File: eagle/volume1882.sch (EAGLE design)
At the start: 39 parts, among them IC1 LM317, IC2 LM337, U1 DS1882, U2 ATMEGA328P_TQFP

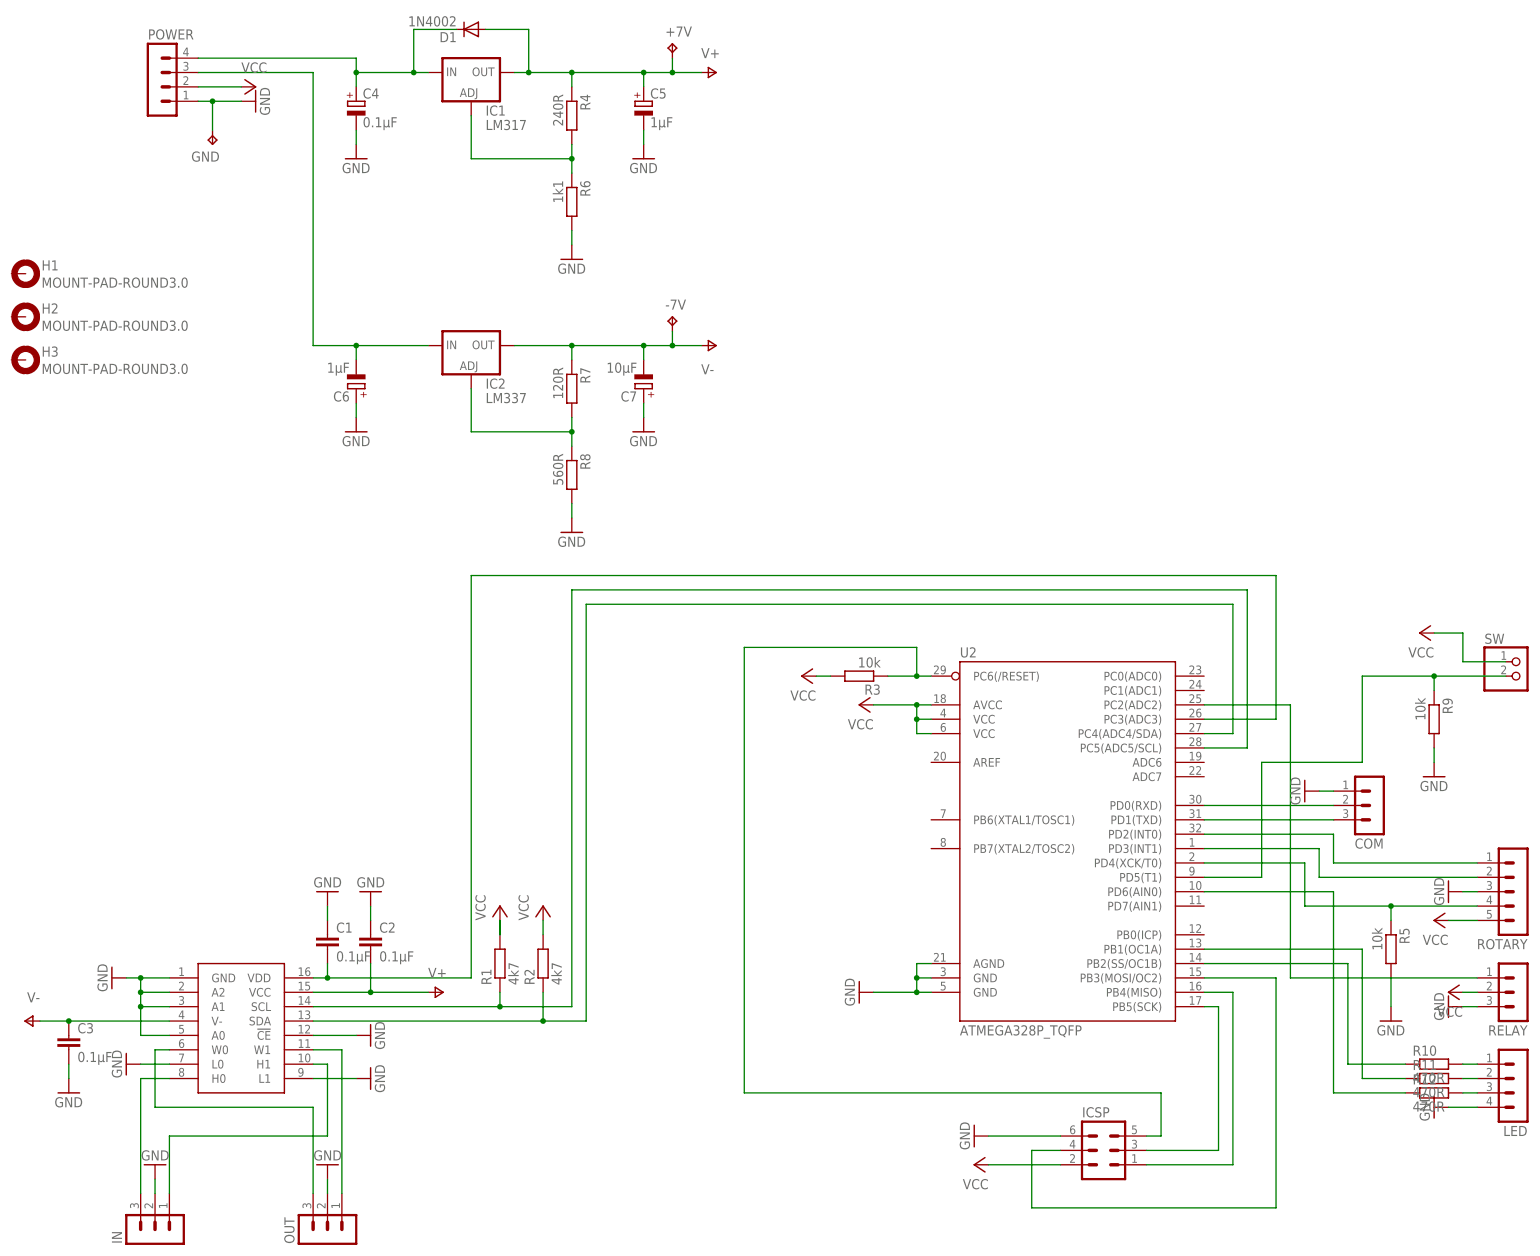
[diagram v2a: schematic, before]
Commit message: fixed wrong size parts
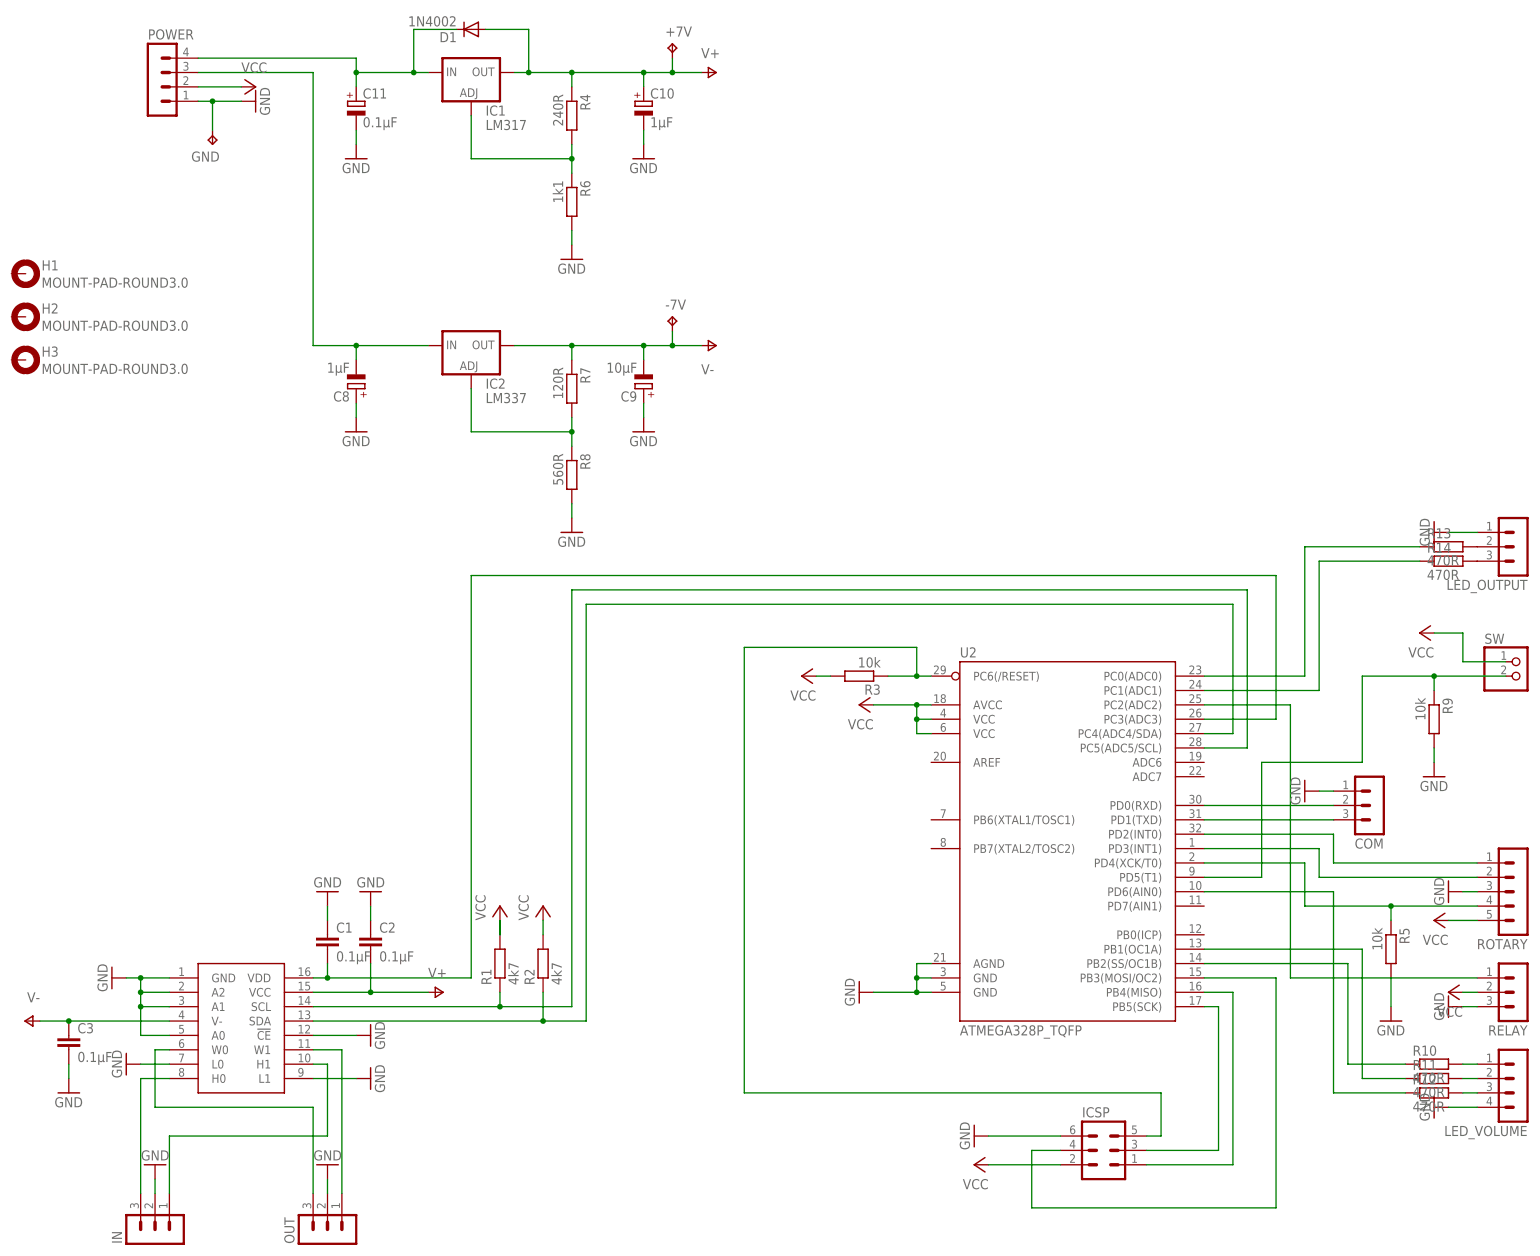
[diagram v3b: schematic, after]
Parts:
- removed C4: 0.1µF, resistor:CPOL-EUE5-5
- removed C5, C6: 1µF, resistor:CPOL-EUE5-5
- removed C7: 10µF, resistor:CPOL-EUE5-5
- added C10, C8: 1µF, resistor:CPOL-EUE2-5
- added C11: 0.1µF, resistor:CPOL-EUE2-5
- added C9: 10µF, resistor:CPOL-EUE2-5
- added LED_OUTPUT: (no value), con-lstb:MA03-1
- added R13, R14: 470R, resistor:R-EU_R1206
- renumbered LED to LED_VOLUME
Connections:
- new net N$29: R13.1, U2.PC0(ADC0)
- new net N$30: R14.1, U2.PC1(ADC1)
- new net N$31: LED_OUTPUT.2, R13.2
- new net N$32: LED_OUTPUT.3, R14.2
- net GND: now also C10.-, C11.-, C8.+, C9.+, LED_OUTPUT.1; no longer C4.-, C5.-, C6.+, C7.+
- net N$20: now also C11.+; no longer C4.+
- net N$21: now also C8.-; no longer C6.-
- net V+: now also C10.+; no longer C5.+
- net V-: now also C9.-; no longer C7.-
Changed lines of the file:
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@@
 <part name="R5" library="resistor" deviceset="R-EU_" device="R1206" value="10k"/>
 <part name="P+9" library="supply1" deviceset="VCC" device=""/>
-<part name="LED" library="con-lstb" deviceset="MA04-1" device=""/>
+<part name="LED_VOLUME" library="con-lstb" deviceset="MA04-1" device=""/>
 <part name="GND11" library="supply1" deviceset="GND" device=""/>
 <part name="IN" library="con-lstb" deviceset="MA03-1" device=""/>
@@
 <part name="IC1" library="v-reg" deviceset="LM317?*" device="MBSTT3" value="LM317"/>
 <part name="POWER" library="con-lstb" deviceset="MA04-1" device=""/>
-<part name="C4" library="resistor" deviceset="CPOL-EU" device="E5-5" value="0.1µF"/>
-<part name="C5" library="resistor" deviceset="CPOL-EU" device="E5-5" value="1µF"/>
 <part name="GND16" library="supply1" deviceset="GND" device=""/>
 <part name="GND17" library="supply1" deviceset="GND" device=""/>
@@
 <part name="P+8" library="supply1" deviceset="VCC" device=""/>
 <part name="IC2" library="lm337" deviceset="LM337" device=""/>
-<part name="C6" library="resistor" deviceset="CPOL-EU" device="E5-5" value="1µF"/>
-<part name="C7" library="resistor" deviceset="CPOL-EU" device="E5-5" value="10µF"/>
 <part name="GND20" library="supply1" deviceset="GND" device=""/>
 <part name="GND21" library="supply1" deviceset="GND" device=""/>
@@
 <part name="+7V" library="testpad" deviceset="TP" device="TP12SQ"/>
 <part name="GND" library="testpad" deviceset="TP" device="TP12SQ"/>
+<part name="LED_OUTPUT" library="con-lstb" deviceset="MA03-1" device=""/>
+<part name="GND25" library="supply1" deviceset="GND" device=""/>
+<part name="R13" library="resistor" deviceset="R-EU_" device="R1206" value="470R"/>
+<part name="R14" library="resistor" deviceset="R-EU_" device="R1206" value="470R"/>
+<part name="C8" library="resistor" deviceset="CPOL-EU" device="E2-5" value="1µF"/>
+<part name="C9" library="resistor" deviceset="CPOL-EU" device="E2-5" value="10µF"/>
+<part name="C10" library="resistor" deviceset="CPOL-EU" device="E2-5" value="1µF"/>
+<part name="C11" library="resistor" deviceset="CPOL-EU" device="E2-5" value="0.1µF"/>
 </parts>
 <sheets>
@@
 <instance part="R5" gate="G$1" x="231.14" y="50.8" rot="R270"/>
 <instance part="P+9" gate="VCC" x="238.76" y="55.88" rot="R90"/>
-<instance part="LED" gate="1" x="254" y="25.4" rot="R180"/>
+<instance part="LED_VOLUME" gate="1" x="254" y="25.4" rot="R180"/>
 <instance part="GND11" gate="1" x="238.76" y="22.86" rot="R270"/>
 <instance part="IN" gate="G$1" x="12.7" y="0" rot="R90"/>
@@
 <instance part="IC1" gate="G$1" x="68.58" y="205.74"/>
 <instance part="POWER" gate="1" x="12.7" y="205.74"/>
-<instance part="C4" gate="G$1" x="48.26" y="200.66"/>
-<instance part="C5" gate="G$1" x="99.06" y="200.66"/>
 <instance part="GND16" gate="1" x="30.48" y="200.66" rot="R90"/>
 <instance part="GND17" gate="1" x="48.26" y="190.5"/>
@@
 <instance part="P+8" gate="VCC" x="30.48" y="203.2" rot="R270"/>
 <instance part="IC2" gate="G$1" x="68.58" y="154.94"/>
-<instance part="C6" gate="G$1" x="48.26" y="149.86" rot="R180"/>
-<instance part="C7" gate="G$1" x="99.06" y="149.86" rot="R180"/>
 <instance part="GND20" gate="1" x="48.26" y="142.24"/>
 <instance part="GND21" gate="1" x="99.06" y="142.24"/>
@@
 <instance part="+7V" gate="G$1" x="104.14" y="210.82"/>
 <instance part="GND" gate="G$1" x="22.86" y="193.04" rot="R180"/>
+<instance part="LED_OUTPUT" gate="G$1" x="254" y="121.92" rot="R180"/>
+<instance part="GND25" gate="1" x="238.76" y="124.46" rot="R270"/>
+<instance part="R13" gate="G$1" x="241.3" y="121.92"/>
+<instance part="R14" gate="G$1" x="241.3" y="119.38"/>
+<instance part="C8" gate="G$1" x="48.26" y="149.86" rot="R180"/>
+<instance part="C9" gate="G$1" x="99.06" y="149.86" rot="R180"/>
+<instance part="C10" gate="G$1" x="99.06" y="200.66"/>
+<instance part="C11" gate="G$1" x="48.26" y="200.66"/>
 </instances>
 <busses>
@@
 </segment>
 <segment>
-<pinref part="LED" gate="1" pin="4"/>
+<pinref part="LED_VOLUME" gate="1" pin="4"/>
 <pinref part="GND11" gate="1" pin="GND"/>
 <wire x1="246.38" y1="22.86" x2="241.3" y2="22.86" width="0.1524" layer="91"/>
@@
 </segment>
 <segment>
-<pinref part="C4" gate="G$1" pin="-"/>
 <pinref part="GND17" gate="1" pin="GND"/>
 <wire x1="48.26" y1="195.58" x2="48.26" y2="193.04" width="0.1524" layer="91"/>
-</segment>
-<segment>
-<pinref part="C5" gate="G$1" pin="-"/>
+<pinref part="C11" gate="G$1" pin="-"/>
+</segment>
+<segment>
 <pinref part="GND18" gate="1" pin="GND"/>
 <wire x1="99.06" y1="195.58" x2="99.06" y2="193.04" width="0.1524" layer="91"/>
+<pinref part="C10" gate="G$1" pin="-"/>
 </segment>
 <segment>
@@
 </segment>
 <segment>
-<pinref part="C6" gate="G$1" pin="+"/>
 <pinref part="GND20" gate="1" pin="GND"/>
 <wire x1="48.26" y1="147.32" x2="48.26" y2="144.78" width="0.1524" layer="91"/>
-</segment>
-<segment>
-<pinref part="C7" gate="G$1" pin="+"/>
+<pinref part="C8" gate="G$1" pin="+"/>
+</segment>
+<segment>
 <pinref part="GND21" gate="1" pin="GND"/>
 <wire x1="99.06" y1="147.32" x2="99.06" y2="144.78" width="0.1524" layer="91"/>
+<pinref part="C9" gate="G$1" pin="+"/>
 </segment>
 <segment>
@@
 <pinref part="GND24" gate="1" pin="GND"/>
 <wire x1="246.38" y1="40.64" x2="243.84" y2="40.64" width="0.1524" layer="91"/>
+</segment>
+<segment>
+<pinref part="GND25" gate="1" pin="GND"/>
+<pinref part="LED_OUTPUT" gate="G$1" pin="1"/>
+<wire x1="241.3" y1="124.46" x2="246.38" y2="124.46" width="0.1524" layer="91"/>
 </segment>
 </net>
@@
 <pinref part="P-2" gate="1" pin="V-"/>
 <wire x1="86.36" y1="157.48" x2="99.06" y2="157.48" width="0.1524" layer="91"/>
-<pinref part="C7" gate="G$1" pin="-"/>
 <wire x1="99.06" y1="157.48" x2="104.14" y2="157.48" width="0.1524" layer="91"/>
 <wire x1="104.14" y1="157.48" x2="109.22" y2="157.48" width="0.1524" layer="91"/>
@@
 <wire x1="104.14" y1="160.02" x2="104.14" y2="157.48" width="0.1524" layer="91"/>
 <junction x="104.14" y="157.48"/>
+<pinref part="C9" gate="G$1" pin="-"/>
 </segment>
 </net>
@@
 <segment>
 <pinref part="IC1" gate="G$1" pin="OUT"/>
-<pinref part="C5" gate="G$1" pin="+"/>
 <wire x1="76.2" y1="205.74" x2="78.74" y2="205.74" width="0.1524" layer="91"/>
 <wire x1="78.74" y1="205.74" x2="86.36" y2="205.74" width="0.1524" layer="91"/>
@@
 <wire x1="104.14" y1="208.28" x2="104.14" y2="205.74" width="0.1524" layer="91"/>
 <junction x="104.14" y="205.74"/>
+<pinref part="C10" gate="G$1" pin="+"/>
 </segment>
 </net>
@@
 <segment>
 <pinref part="POWER" gate="1" pin="4"/>
-<pinref part="C4" gate="G$1" pin="+"/>
 <wire x1="20.32" y1="208.28" x2="48.26" y2="208.28" width="0.1524" layer="91"/>
 <wire x1="48.26" y1="208.28" x2="48.26" y2="205.74" width="0.1524" layer="91"/>
@@
 <wire x1="58.42" y1="213.36" x2="58.42" y2="205.74" width="0.1524" layer="91"/>
 <junction x="58.42" y="205.74"/>
+<pinref part="C11" gate="G$1" pin="+"/>
 </segment>
 </net>
@@
 <pinref part="IC2" gate="G$1" pin="IN"/>
 <wire x1="40.64" y1="157.48" x2="48.26" y2="157.48" width="0.1524" layer="91"/>
-<pinref part="C6" gate="G$1" pin="-"/>
 <wire x1="48.26" y1="157.48" x2="60.96" y2="157.48" width="0.1524" layer="91"/>
 <wire x1="48.26" y1="154.94" x2="48.26" y2="157.48" width="0.1524" layer="91"/>
 <junction x="48.26" y="157.48"/>
+<pinref part="C8" gate="G$1" pin="-"/>
 </segment>
 </net>
@@
 <segment>
 <pinref part="R10" gate="G$1" pin="2"/>
-<pinref part="LED" gate="1" pin="1"/>
+<pinref part="LED_VOLUME" gate="1" pin="1"/>
 <wire x1="243.84" y1="30.48" x2="246.38" y2="30.48" width="0.1524" layer="91"/>
 </segment>
@@
 <segment>
 <pinref part="R11" gate="G$1" pin="2"/>
-<pinref part="LED" gate="1" pin="2"/>
+<pinref part="LED_VOLUME" gate="1" pin="2"/>
 <wire x1="243.84" y1="27.94" x2="246.38" y2="27.94" width="0.1524" layer="91"/>
 </segment>
@@
 <segment>
 <pinref part="R12" gate="G$1" pin="2"/>
-<pinref part="LED" gate="1" pin="3"/>
+<pinref part="LED_VOLUME" gate="1" pin="3"/>
 <wire x1="243.84" y1="25.4" x2="246.38" y2="25.4" width="0.1524" layer="91"/>
 </segment>
 </net>
+<net name="N$29" class="0">
+<segment>
+<pinref part="U2" gate="U$1" pin="PC0(ADC0)"/>
+<wire x1="198.12" y1="99.06" x2="215.9" y2="99.06" width="0.1524" layer="91"/>
+<wire x1="215.9" y1="99.06" x2="215.9" y2="121.92" width="0.1524" layer="91"/>
+<pinref part="R13" gate="G$1" pin="1"/>
+<wire x1="215.9" y1="121.92" x2="236.22" y2="121.92" width="0.1524" layer="91"/>
+</segment>
+</net>
+<net name="N$30" class="0">
+<segment>
+<pinref part="U2" gate="U$1" pin="PC1(ADC1)"/>
+<wire x1="198.12" y1="96.52" x2="218.44" y2="96.52" width="0.1524" layer="91"/>
+<wire x1="218.44" y1="96.52" x2="218.44" y2="119.38" width="0.1524" layer="91"/>
+<pinref part="R14" gate="G$1" pin="1"/>
+<wire x1="218.44" y1="119.38" x2="236.22" y2="119.38" width="0.1524" layer="91"/>
+</segment>
+</net>
+<net name="N$31" class="0">
+<segment>
+<pinref part="LED_OUTPUT" gate="G$1" pin="2"/>
+<pinref part="R13" gate="G$1" pin="2"/>
+</segment>
+</net>
+<net name="N$32" class="0">
+<segment>
+<pinref part="LED_OUTPUT" gate="G$1" pin="3"/>
+<pinref part="R14" gate="G$1" pin="2"/>
+</segment>
+</net>

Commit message: small fixes
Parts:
- added REMOTE: (no value), con-lstb:MA03-1
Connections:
- new net N$33: REMOTE.1, U2.PB0(ICP)
- net GND: now also REMOTE.2
- net VCC: now also REMOTE.3
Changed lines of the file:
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@@
 <part name="C10" library="resistor" deviceset="CPOL-EU" device="E2-5" value="1µF"/>
 <part name="C11" library="resistor" deviceset="CPOL-EU" device="E2-5" value="0.1µF"/>
+<part name="REMOTE" library="con-lstb" deviceset="MA03-1" device=""/>
+<part name="GND26" library="supply1" deviceset="GND" device=""/>
+<part name="P+12" library="supply1" deviceset="VCC" device=""/>
 </parts>
 <sheets>
@@
 <instance part="C10" gate="G$1" x="99.06" y="200.66"/>
 <instance part="C11" gate="G$1" x="48.26" y="200.66"/>
+<instance part="REMOTE" gate="G$1" x="254" y="10.16" rot="R180"/>
+<instance part="GND26" gate="1" x="241.3" y="10.16" rot="R270"/>
+<instance part="P+12" gate="VCC" x="241.3" y="7.62" rot="R90"/>
 </instances>
 <busses>
@@
 <wire x1="241.3" y1="124.46" x2="246.38" y2="124.46" width="0.1524" layer="91"/>
 </segment>
+<segment>
+<pinref part="REMOTE" gate="G$1" pin="2"/>
+<pinref part="GND26" gate="1" pin="GND"/>
+<wire x1="246.38" y1="10.16" x2="243.84" y2="10.16" width="0.1524" layer="91"/>
+</segment>
 </net>
 <net name="V-" class="0">
@@
 <pinref part="P+11" gate="VCC" pin="VCC"/>
 <wire x1="246.38" y1="43.18" x2="243.84" y2="43.18" width="0.1524" layer="91"/>
+</segment>
+<segment>
+<pinref part="REMOTE" gate="G$1" pin="3"/>
+<pinref part="P+12" gate="VCC" pin="VCC"/>
+<wire x1="246.38" y1="7.62" x2="243.84" y2="7.62" width="0.1524" layer="91"/>
 </segment>
 </net>
@@
 </segment>
 </net>
+<net name="N$33" class="0">
+<segment>
+<pinref part="REMOTE" gate="G$1" pin="1"/>
+<wire x1="246.38" y1="12.7" x2="205.74" y2="12.7" width="0.1524" layer="91"/>
+<wire x1="205.74" y1="12.7" x2="205.74" y2="53.34" width="0.1524" layer="91"/>
+<pinref part="U2" gate="U$1" pin="PB0(ICP)"/>
+<wire x1="205.74" y1="53.34" x2="198.12" y2="53.34" width="0.1524" layer="91"/>
+</segment>
+</net>
